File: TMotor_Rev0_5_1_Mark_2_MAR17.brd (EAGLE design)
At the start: 88.9 x 79.4 mm, 64 parts, among them U10 DEV-16771, U3 INA125U, U4 INA125U, U5 SN65HVD230MDREP

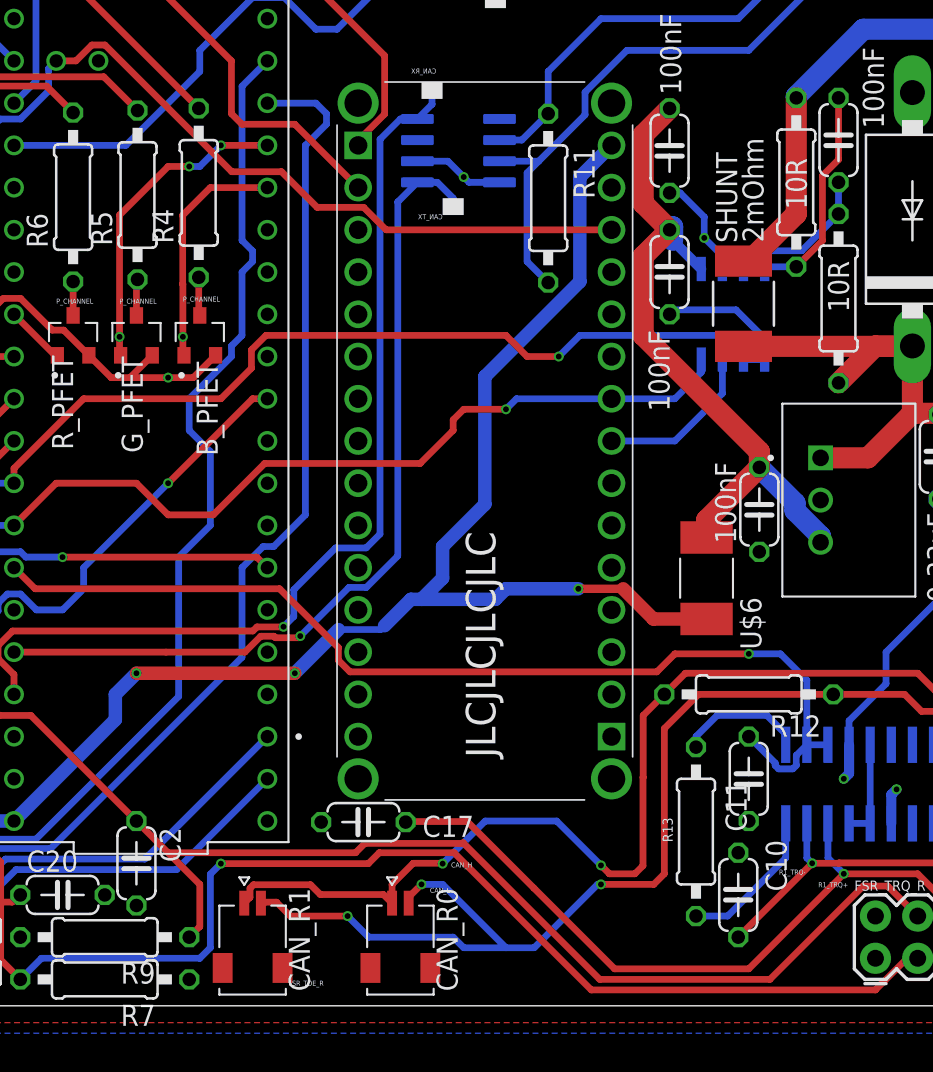
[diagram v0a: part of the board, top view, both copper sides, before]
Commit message: GND and 3.3V trace widths (copper pour) improved.
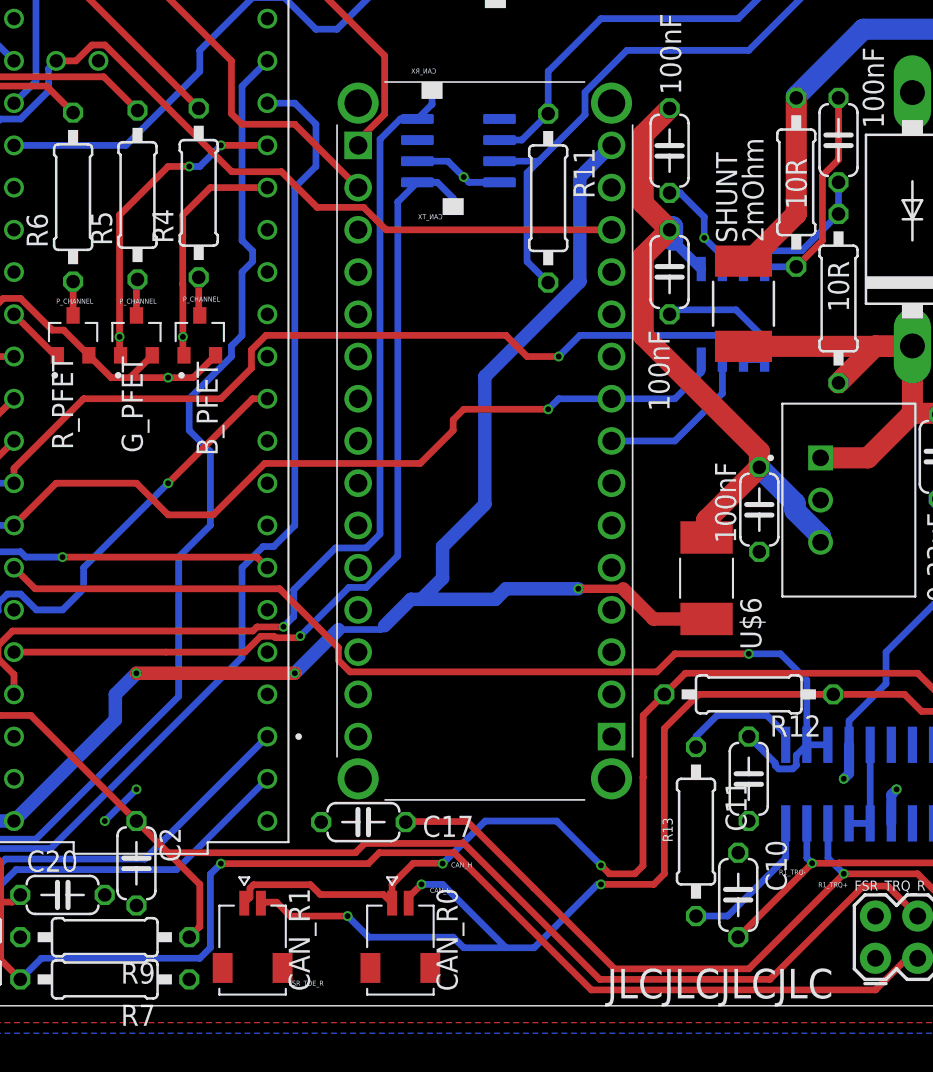
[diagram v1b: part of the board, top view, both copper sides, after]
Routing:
- net GND: track 83.3 -> 86.0 mm, vias 9 -> 11
- net COPI: track 64.9 -> 63.6 mm
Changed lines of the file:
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@@
 <vertex x="13.97" y="19.05"/>
 </polygon>
-<text x="3.81" y="19.685" size="1.778" layer="121" rot="R90">JLCJLCJLCJLC</text>
+<text x="24.13" y="6.985" size="1.778" layer="121" rot="R180">JLCJLCJLCJLC</text>
 <polygon width="0" layer="121">
 <vertex x="-0.635" y="60.325"/>
@@
 </polygon>
 <polygon width="0.4064" layer="42">
-<vertex x="-12.065" y="8.255"/>
-<vertex x="-12.065" y="12.7"/>
+<vertex x="-13.97" y="8.255"/>
+<vertex x="-13.97" y="12.7"/>
 <vertex x="-6.35" y="12.7"/>
 <vertex x="-5.715" y="12.065"/>
@@
 <vertex x="0.635" y="13.97"/>
 <vertex x="1.27" y="13.335"/>
-<vertex x="0.635" y="12.7"/>
 <vertex x="0" y="12.065"/>
-<vertex x="0" y="11.43"/>
 <vertex x="0" y="8.89"/>
 <vertex x="-3.81" y="8.89"/>
 <vertex x="-4.445" y="9.525"/>
-<vertex x="-5.715" y="9.525"/>
 <vertex x="-8.255" y="9.525"/>
 <vertex x="-9.525" y="8.255"/>
@@
 </polygon>
 <polygon width="0.1524" layer="42">
-<vertex x="29.21" y="71.12"/>
+<vertex x="29.21" y="68.58"/>
 <vertex x="29.21" y="72.39"/>
 <vertex x="25.4" y="76.2"/>
-<vertex x="21.59" y="76.2"/>
 <vertex x="19.685" y="76.2"/>
 <vertex x="19.05" y="75.565"/>
@@
 <vertex x="17.145" y="78.105"/>
 <vertex x="17.145" y="79.375"/>
-<vertex x="18.415" y="80.645"/>
 <vertex x="19.05" y="81.28"/>
 <vertex x="22.225" y="81.28"/>
 <vertex x="22.225" y="78.74"/>
 <vertex x="26.035" y="78.74"/>
-<vertex x="26.67" y="78.105"/>
 <vertex x="32.385" y="72.39"/>
-<vertex x="32.385" y="69.85"/>
-<vertex x="29.845" y="69.85"/>
-<vertex x="29.21" y="69.85"/>
+<vertex x="32.385" y="68.58"/>
 </polygon>
 <polygon width="0.1524" layer="42">
@@
 <vertex x="26.035" y="81.28"/>
 <vertex x="26.035" y="81.915"/>
+</polygon>
+<polygon width="0.1524" layer="42">
+<vertex x="29.845" y="77.47"/>
+<vertex x="29.845" y="67.945"/>
+<vertex x="31.115" y="66.675"/>
+<vertex x="31.115" y="27.305"/>
+<vertex x="29.845" y="26.035"/>
+<vertex x="14.605" y="26.035"/>
+<vertex x="11.43" y="22.86"/>
+<vertex x="11.43" y="15.24"/>
+<vertex x="10.16" y="15.24"/>
+<vertex x="10.16" y="10.795"/>
+<vertex x="13.97" y="10.795"/>
+<vertex x="15.24" y="12.065"/>
+<vertex x="15.24" y="20.955"/>
+<vertex x="16.51" y="22.225"/>
+<vertex x="27.94" y="22.225"/>
+<vertex x="29.21" y="20.955"/>
+<vertex x="33.02" y="20.955"/>
+<vertex x="36.195" y="24.13"/>
+<vertex x="36.195" y="67.945"/>
+<vertex x="34.29" y="69.85"/>
+<vertex x="34.29" y="80.645"/>
+<vertex x="30.48" y="80.645"/>
+<vertex x="29.845" y="81.28"/>
+<vertex x="27.305" y="81.28"/>
+<vertex x="27.305" y="79.375"/>
+<vertex x="27.94" y="79.375"/>
 </polygon>
 </plain>
@@
 <wire x1="38.735" y1="47.3075" x2="41.91" y2="47.3075" width="1.27" layer="16"/>
 <wire x1="30.48" y1="35.2425" x2="42.2275" y2="35.2425" width="1.27" layer="16"/>
+<via x="-19.685" y="15.875" extent="1-16" drill="0.35"/>
+<wire x1="-19.685" y1="15.875" x2="-17.8026" y2="17.7574" width="0.4064" layer="16"/>
+<wire x1="-17.8026" y1="17.7574" x2="-17.8026" y2="17.78" width="0.4064" layer="16"/>
+<via x="-17.78" y="17.78" extent="1-16" drill="0.35"/>
 </signal>
 <signal name="VIN">
@@
 <wire x1="1.27" y1="39.37" x2="1.27" y2="40.005" width="0.4064" layer="1"/>
 <wire x1="1.27" y1="40.005" x2="1.905" y2="40.64" width="0.4064" layer="1"/>
-<wire x1="1.905" y1="40.64" x2="4.445" y2="40.64" width="0.4064" layer="1"/>
-<via x="4.445" y="40.64" extent="1-16" drill="0.35"/>
-<wire x1="5.08" y1="41.275" x2="10.795" y2="41.275" width="0.4064" layer="16"/>
-<wire x1="5.08" y1="41.275" x2="4.445" y2="40.64" width="0.4064" layer="16"/>
+<wire x1="1.905" y1="40.64" x2="6.985" y2="40.64" width="0.4064" layer="1"/>
+<via x="6.985" y="40.64" extent="1-16" drill="0.35"/>
+<wire x1="7.62" y1="41.275" x2="10.795" y2="41.275" width="0.4064" layer="16"/>
+<wire x1="7.62" y1="41.275" x2="6.985" y2="40.64" width="0.4064" layer="16"/>
 <wire x1="-22.606" y1="36.195" x2="-17.78" y2="36.195" width="0.4064" layer="1"/>
 <wire x1="-0.7169" y1="37.3831" x2="1.27" y2="39.37" width="0.4064" layer="1"/>
@@
 <wire x1="-11.43" y1="31.115" x2="-10.16" y2="32.385" width="0.4064" layer="16"/>
 <wire x1="-10.16" y1="32.385" x2="-9.525" y2="32.385" width="0.4064" layer="16"/>
-<wire x1="-9.525" y1="32.385" x2="-7.62" y2="34.29" width="0.4064" layer="16"/>
-<wire x1="-7.62" y1="56.515" x2="-6.35" y2="57.785" width="0.4064" layer="16"/>
-<wire x1="-6.35" y1="57.785" x2="-6.35" y2="58.42" width="0.4064" layer="16"/>
-<wire x1="-6.35" y1="58.42" x2="-6.985" y2="59.055" width="0.4064" layer="16"/>
-<wire x1="-7.62" y1="34.29" x2="-7.62" y2="56.515" width="0.4064" layer="16"/>
-<wire x1="-6.985" y1="59.055" x2="-9.906" y2="59.055" width="0.4064" layer="16"/>
+<wire x1="-9.525" y1="32.385" x2="-8.255" y2="33.655" width="0.4064" layer="16"/>
+<wire x1="-8.255" y1="53.975" x2="-6.985" y2="55.245" width="0.4064" layer="16"/>
+<wire x1="-6.985" y1="55.245" x2="-6.985" y2="57.785" width="0.4064" layer="16"/>
+<wire x1="-6.985" y1="57.785" x2="-8.255" y2="59.055" width="0.4064" layer="16"/>
+<wire x1="-8.255" y1="33.655" x2="-8.255" y2="53.975" width="0.4064" layer="16"/>
+<wire x1="-8.255" y1="59.055" x2="-9.906" y2="59.055" width="0.4064" layer="16"/>
 </signal>
 <signal name="CIPO">

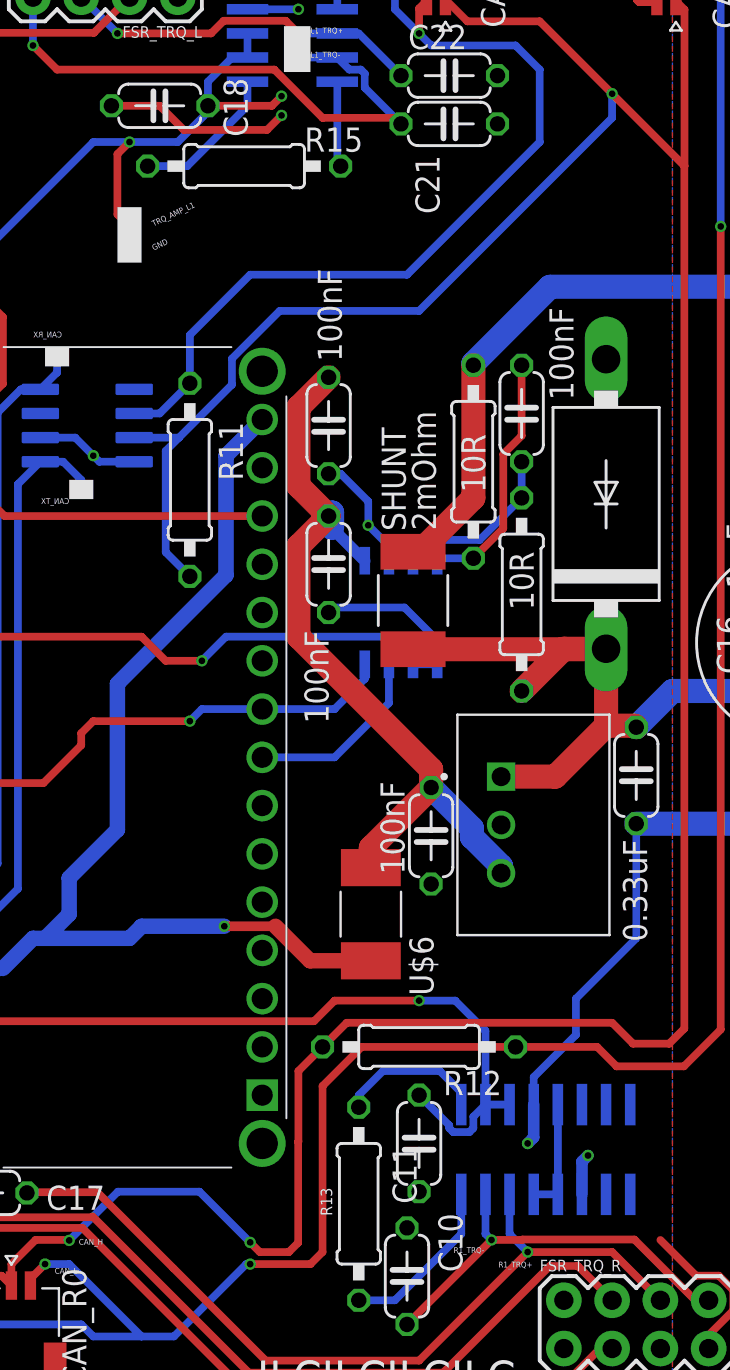
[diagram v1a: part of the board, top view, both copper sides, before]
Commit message: Improved CAN bus termination resistor placement
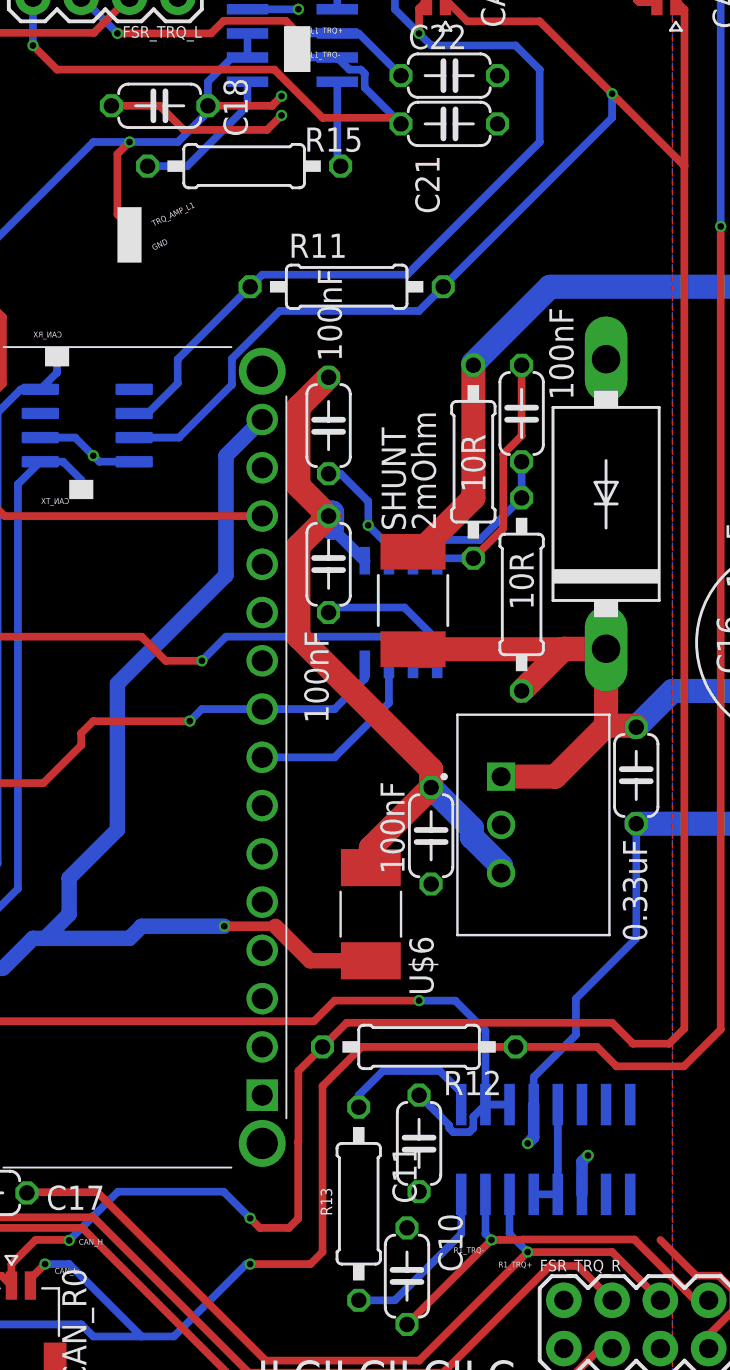
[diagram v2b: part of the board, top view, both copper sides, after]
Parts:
- moved R11 13.1 mm to (15.2, 63.5), turned to 0 degrees
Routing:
- net N$44: track 173.6 -> 163.6 mm
- net N$45: track 188.5 -> 187.9 mm
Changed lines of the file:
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@@
 <attribute name="VALUE" x="-28.1305" y="22.0345" size="0.6096" layer="27" font="vector" ratio="20" rot="R90"/>
 </element>
-<element name="R11" library="rcl" library_urn="urn:adsk.eagle:library:334" package="0207/10" package3d_urn="urn:adsk.eagle:package:23491/2" value="120R" x="6.985" y="53.34" smashed="yes" rot="R270">
-<attribute name="NAME" x="8.509" y="56.388" size="1.27" layer="25" ratio="10" rot="R270"/>
-<attribute name="POPULARITY" value="36" x="6.985" y="53.34" size="1.778" layer="27" rot="R270" display="off"/>
-<attribute name="SPICEPREFIX" value="R" x="6.985" y="53.34" size="1.778" layer="27" rot="R270" display="off"/>
-<attribute name="VALUE" x="6.35" y="55.6006" size="1.27" layer="27" ratio="10" rot="R270"/>
+<element name="R11" library="rcl" library_urn="urn:adsk.eagle:library:334" package="0207/10" package3d_urn="urn:adsk.eagle:package:23491/2" value="120R" x="15.24" y="63.5" smashed="yes">
+<attribute name="NAME" x="12.192" y="65.024" size="1.27" layer="25" ratio="10"/>
+<attribute name="POPULARITY" value="36" x="15.24" y="63.5" size="1.778" layer="27" display="off"/>
+<attribute name="SPICEPREFIX" value="R" x="15.24" y="63.5" size="1.778" layer="27" display="off"/>
+<attribute name="VALUE" x="12.9794" y="62.865" size="1.27" layer="27" ratio="10"/>
 </element>
 <element name="R12" library="rcl" library_urn="urn:adsk.eagle:library:334" package="0207/10" package3d_urn="urn:adsk.eagle:package:23491/2" value="120R" x="19.05" y="23.495" smashed="yes" rot="R180">
@@
 <contactref element="R11" pad="2"/>
 <contactref element="R12" pad="2"/>
-<wire x1="12.6873" y1="13.1873" x2="12.6873" y2="18.4973" width="0.4064" layer="1"/>
+<wire x1="12.6873" y1="14.4573" x2="12.6873" y2="18.4973" width="0.4064" layer="1"/>
 <wire x1="12.6873" y1="18.4973" x2="12.7" y2="18.51" width="0.4064" layer="1"/>
-<wire x1="10.16" y1="13.208" x2="10.668" y2="12.7" width="0.4064" layer="1"/>
-<via x="10.16" y="13.208" extent="1-16" drill="0.35"/>
+<wire x1="10.16" y1="14.478" x2="10.668" y2="13.97" width="0.4064" layer="1"/>
+<via x="10.16" y="14.478" extent="1-16" drill="0.35"/>
 <wire x1="29.21" y1="24.765" x2="15.24" y2="24.765" width="0.4064" layer="1"/>
 <wire x1="15.24" y1="24.765" x2="13.97" y2="23.495" width="0.4064" layer="1"/>
-<wire x1="12.2" y1="12.7" x2="12.6873" y2="13.1873" width="0.4064" layer="1"/>
-<wire x1="10.668" y1="12.7" x2="12.2" y2="12.7" width="0.4064" layer="1"/>
+<wire x1="12.2" y1="13.97" x2="12.6873" y2="14.4573" width="0.4064" layer="1"/>
+<wire x1="10.668" y1="13.97" x2="12.2" y2="13.97" width="0.4064" layer="1"/>
 <wire x1="-11.295" y1="10.937" x2="-10.9506" y2="11.2814" width="0.4064" layer="1"/>
 <wire x1="-10.9506" y1="11.2814" x2="-10.9506" y2="11.83429375" width="0.4064" layer="1"/>
@@
 <wire x1="-10.74229375" y1="12.0426" x2="-7.30770625" y2="12.0426" width="0.4064" layer="1"/>
 <wire x1="-7.30770625" y1="12.0426" x2="-6.71770625" y2="11.4526" width="0.4064" layer="1"/>
-<wire x1="6.985" y1="48.26" x2="5.715" y2="49.53" width="0.4064" layer="16"/>
 <wire x1="33.011" y1="69.859" x2="33.011" y2="24.4610125" width="0.4064" layer="1"/>
 <wire x1="33.011" y1="24.4610125" x2="32.21499375" y2="23.66500625" width="0.4064" layer="1"/>
@@
 <wire x1="0.635" y1="13.335" x2="0.635" y2="13.3124" width="0.4064" layer="1"/>
 <via x="0.635" y="13.3124" extent="1-16" drill="0.35"/>
-<wire x1="3.1976" y1="15.875" x2="7.493" y2="15.875" width="0.4064" layer="16"/>
-<wire x1="10.16" y1="13.208" x2="7.493" y2="15.875" width="0.4064" layer="16"/>
+<wire x1="3.1976" y1="15.875" x2="8.763" y2="15.875" width="0.4064" layer="16"/>
+<wire x1="10.16" y1="14.478" x2="8.763" y2="15.875" width="0.4064" layer="16"/>
 <wire x1="0.635" y1="13.3124" x2="3.1976" y2="15.875" width="0.4064" layer="16"/>
 <wire x1="12.7" y1="22.225" x2="13.97" y2="23.495" width="0.4064" layer="1"/>
@@
 <wire x1="21.59" y1="77.47" x2="20.5205" y2="78.5395" width="0.4064" layer="1"/>
 <wire x1="20.5205" y1="78.5395" x2="20.439" y2="78.5395" width="0.4064" layer="1"/>
-<wire x1="5.715" y1="54.8616375" x2="6.4158625" y2="55.5625" width="0.4064" layer="16"/>
 <wire x1="6.4158625" y1="55.5625" x2="9.2019" y2="58.3485375" width="0.4064" layer="16"/>
-<wire x1="5.715" y1="49.53" x2="5.715" y2="54.8616375" width="0.4064" layer="16"/>
 <wire x1="6.4158625" y1="55.5625" x2="4.0575" y2="55.5625" width="0.4064" layer="16"/>
 <wire x1="25.4" y1="77.47" x2="21.59" y2="77.47" width="0.4064" layer="1"/>
@@
 <wire x1="29.21" y1="72.39" x2="29.21" y2="73.66" width="0.4064" layer="16"/>
 <via x="29.21" y="73.66" extent="1-16" drill="0.35"/>
-<wire x1="19.05" y1="62.23" x2="29.21" y2="72.39" width="0.4064" layer="16"/>
+<wire x1="19.05" y1="62.23" x2="20.32" y2="63.5" width="0.4064" layer="16"/>
 <wire x1="32.5675" y1="78.5395" x2="33.02" y2="78.087" width="0.4064" layer="1"/>
 <wire x1="33.02" y1="69.868" x2="33.011" y2="69.859" width="0.4064" layer="1"/>
 <wire x1="33.02" y1="78.087" x2="33.02" y2="69.868" width="0.4064" layer="1"/>
+<wire x1="20.32" y1="63.5" x2="29.21" y2="72.39" width="0.4064" layer="16"/>
 </signal>
 <signal name="N$45">
@@
 <wire x1="10.16" y1="12.065" x2="9.95605625" y2="12.065" width="0.4064" layer="16"/>
 <wire x1="9.95605625" y1="12.065" x2="6.14605625" y2="8.255" width="0.4064" layer="16"/>
-<wire x1="6.985" y1="58.42" x2="5.3975" y2="56.8325" width="0.4064" layer="16"/>
-<wire x1="5.3975" y1="56.8325" x2="4.0575" y2="56.8325" width="0.4064" layer="16"/>
+<wire x1="10.16" y1="63.5" x2="6.35" y2="59.69" width="0.4064" layer="16"/>
+<wire x1="6.35" y1="59.69" x2="6.35" y2="58.42" width="0.4064" layer="16"/>
+<wire x1="4.0575" y1="56.8325" x2="4.1275" y2="56.7625" width="0.4064" layer="16"/>
 <wire x1="4.445" y1="8.255" x2="0.635" y2="12.065" width="0.4064" layer="16"/>
 <wire x1="0.635" y1="12.065" x2="-0.635" y2="12.065" width="0.4064" layer="16"/>
@@
 <wire x1="19.05" y1="78.1505" x2="19.439" y2="78.5395" width="0.4064" layer="1"/>
 <wire x1="19.05" y1="76.835" x2="17.78" y2="78.105" width="0.4064" layer="16"/>
-<wire x1="6.985" y1="58.42" x2="6.985" y2="60.96" width="0.4064" layer="16"/>
-<wire x1="6.985" y1="60.96" x2="10.16" y2="64.135" width="0.4064" layer="16"/>
+<wire x1="10.16" y1="63.5" x2="10.795" y2="64.135" width="0.4064" layer="16"/>
 <wire x1="18.415" y1="64.135" x2="25.4" y2="71.12" width="0.4064" layer="16"/>
 <wire x1="25.4" y1="71.12" x2="25.4" y2="74.93" width="0.4064" layer="16"/>
 <wire x1="25.4" y1="74.93" x2="24.13" y2="76.2" width="0.4064" layer="16"/>
 <wire x1="19.685" y1="76.2" x2="19.05" y2="76.835" width="0.4064" layer="16"/>
-<wire x1="10.16" y1="64.135" x2="18.415" y2="64.135" width="0.4064" layer="16"/>
+<wire x1="10.795" y1="64.135" x2="18.415" y2="64.135" width="0.4064" layer="16"/>
 <wire x1="24.13" y1="76.2" x2="19.685" y2="76.2" width="0.4064" layer="16"/>
+<wire x1="6.35" y1="58.42" x2="4.7625" y2="56.8325" width="0.4064" layer="16"/>
+<wire x1="4.7625" y1="56.8325" x2="4.0575" y2="56.8325" width="0.4064" layer="16"/>
 </signal>
 <signal name="CANTX">
